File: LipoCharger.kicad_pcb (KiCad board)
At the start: 4 copper layers, 43.5 x 36 mm, 34 parts, among them J1 S2B-XH-A, J2 USB_C_Receptacle_USB2.0_14P, Q1 SI2300A, Q2 SI2300A, SW1 SK12D07VG4, U1 TP4056-42-ESOP8, U2 MT3608, U3 FM2113

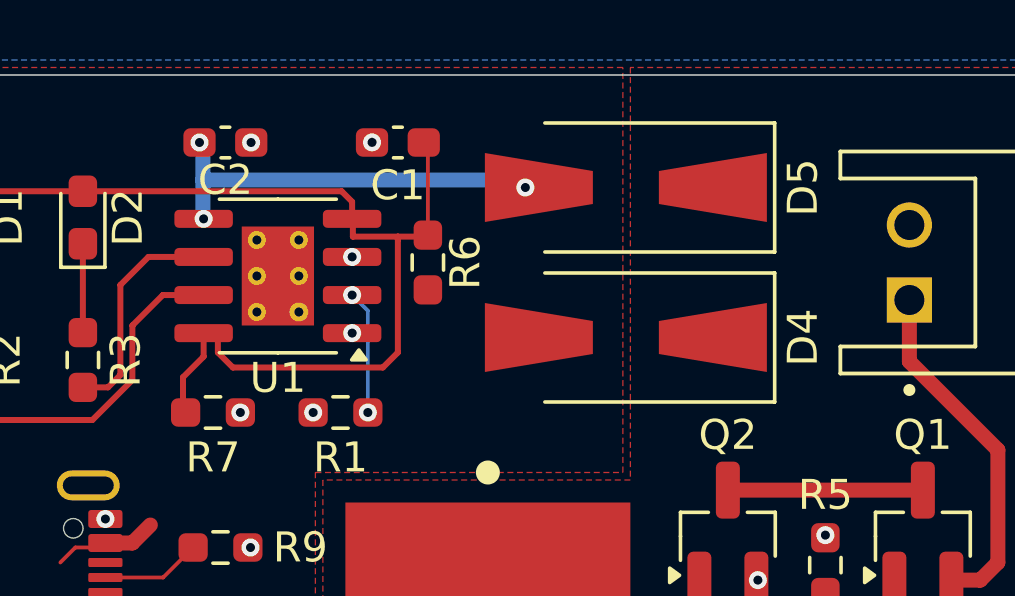
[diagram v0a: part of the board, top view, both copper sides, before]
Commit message: Updated to add power pathing for usb and charging ic
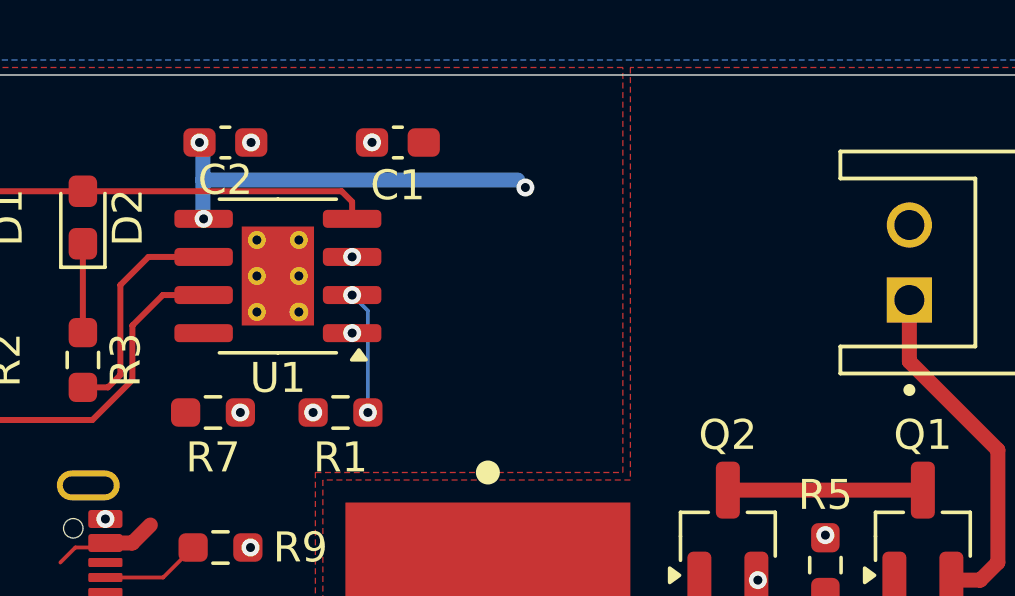
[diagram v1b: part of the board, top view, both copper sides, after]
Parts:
- removed D4, D5: B340A, Diode_SMD:D_SMA-SMB_Universal_Handsoldering
- removed R6: 0.4, Resistor_SMD:R_0603_1608Metric_Pad0.98x0.95mm_HandSolder
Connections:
- C1 pad 1: Net-(D1-A) -> VBUS
- C2 pad 1: Net-(D5-A) -> +BATT
- D1 pad 2: Net-(D1-A) -> VBUS
- D2 pad 2: Net-(D1-A) -> VBUS
- R7 pad 1: Net-(D1-A) -> VBUS
- U1 pad 4: Net-(D1-A) -> VBUS
- U1 pad 5: Net-(D5-A) -> +BATT
- U1 pad 8: Net-(D1-A) -> VBUS
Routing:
- net Net-(D1-A): track 34.2 -> 0.00 mm
- net VBUS: track 7.43 -> 21.9 mm
- net Net-(D5-A): track 13.6 -> 0.00 mm, vias 3 -> 0
- net +BATT: track 6.47 -> 20.1 mm, vias 0 -> 3

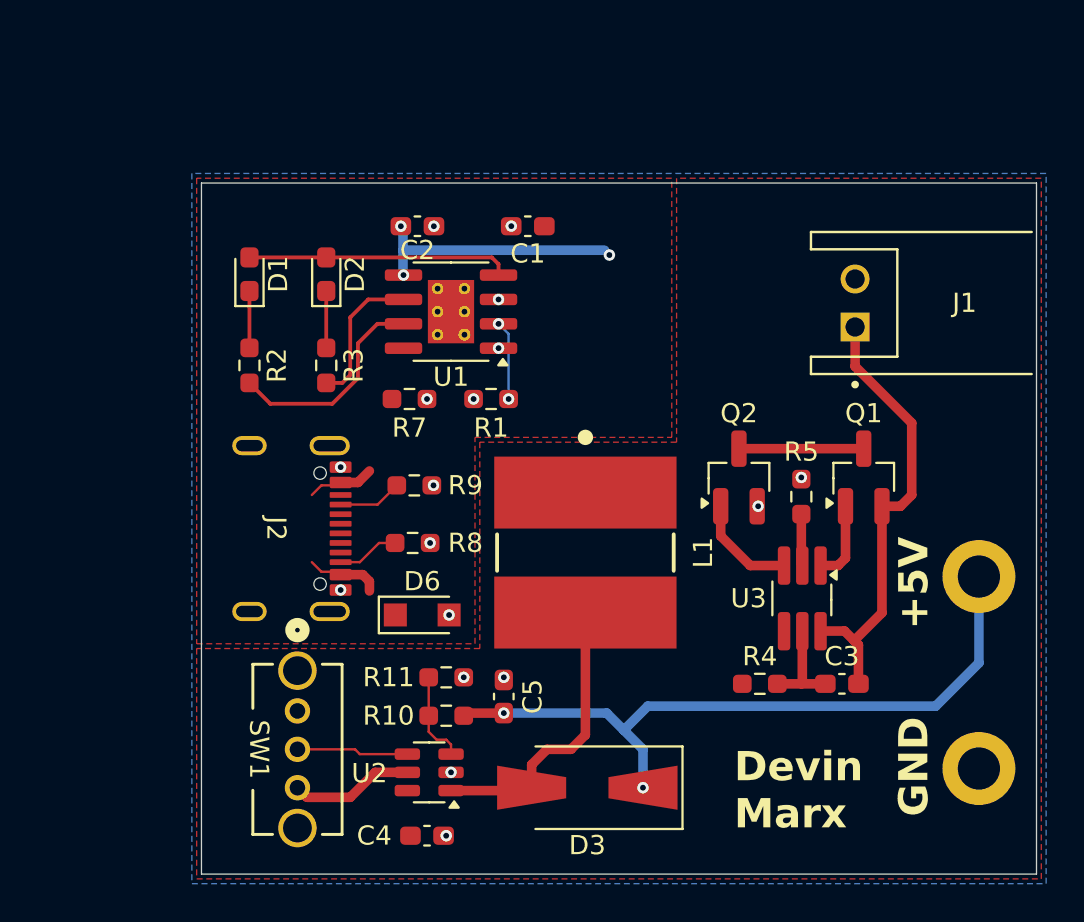
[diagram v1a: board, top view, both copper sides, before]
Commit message: added the updated inductor and update the model for the PMOS mosfet (Should update the NMOS)
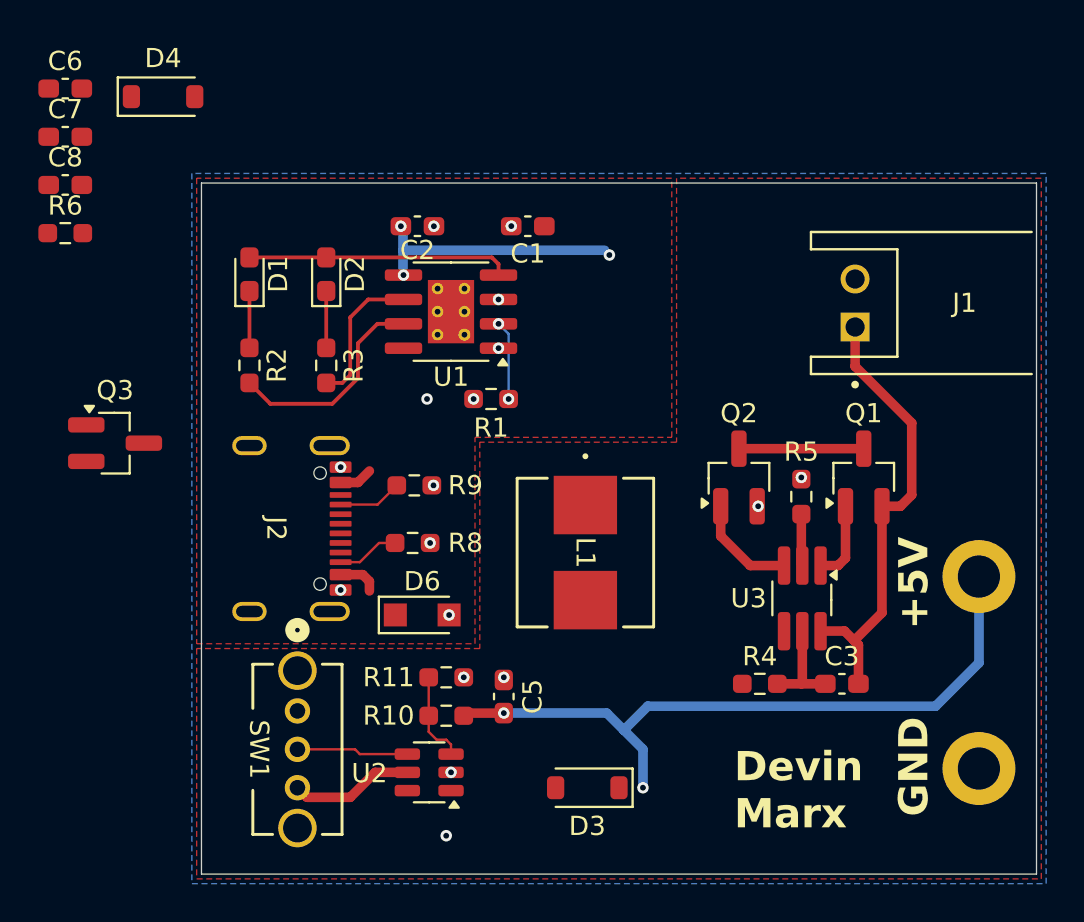
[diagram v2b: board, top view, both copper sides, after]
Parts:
- removed C4: 22uF, Capacitor_SMD:C_0603_1608Metric_Pad1.08x0.95mm_HandSolder
- removed R7: 10k, Resistor_SMD:R_0603_1608Metric_Pad0.98x0.95mm_HandSolder
- added C6: 100nF, Capacitor_SMD:C_0603_1608Metric_Pad1.08x0.95mm_HandSolder, F.Cu at (22.9, 19.6)
- added C7: 100nF, Capacitor_SMD:C_0603_1608Metric_Pad1.08x0.95mm_HandSolder, F.Cu at (22.9, 22.1)
- added C8: 22uF, Capacitor_SMD:C_0603_1608Metric_Pad1.08x0.95mm_HandSolder, F.Cu at (22.9, 24.6)
- added D4: MBR230LSFT1G, Diode_SMD:D_SOD-123, F.Cu at (28.0, 20.0)
- added Q3: HL 2305A, Package_TO_SOT_SMD:SOT-23_Handsoldering, F.Cu at (25.5, 38.0)
- added R6: 10k, Resistor_SMD:R_0603_1608Metric_Pad0.98x0.95mm_HandSolder, F.Cu at (22.9, 27.1)
- C1, C2: value 10uF -> 22uF
- C3: value 0.1uF -> 100nF
- D3: value SS34 -> MBR230LSFT1G; footprint Diode_SMD:D_SMA-SMB_Universal_Handsoldering -> Diode_SMD:D_SOD-123
- L1: value 22uH -> 10uH; footprint a_Library:WE-PD2_1054 -> a_Library:HY0630-100M-M
- R10: value 73.2k -> 82k
- R11: value 10k -> 11k
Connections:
- L1 pad 1: +BATT -> Net-(D4-K)
- U2 pad 5: +BATT -> Net-(D4-K)
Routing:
- net Net-(D3-A): track 14.1 -> 0.00 mm
- net VBUS: track 21.9 -> 18.8 mm

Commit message: Reoriented the PCB for the updated schematic layout
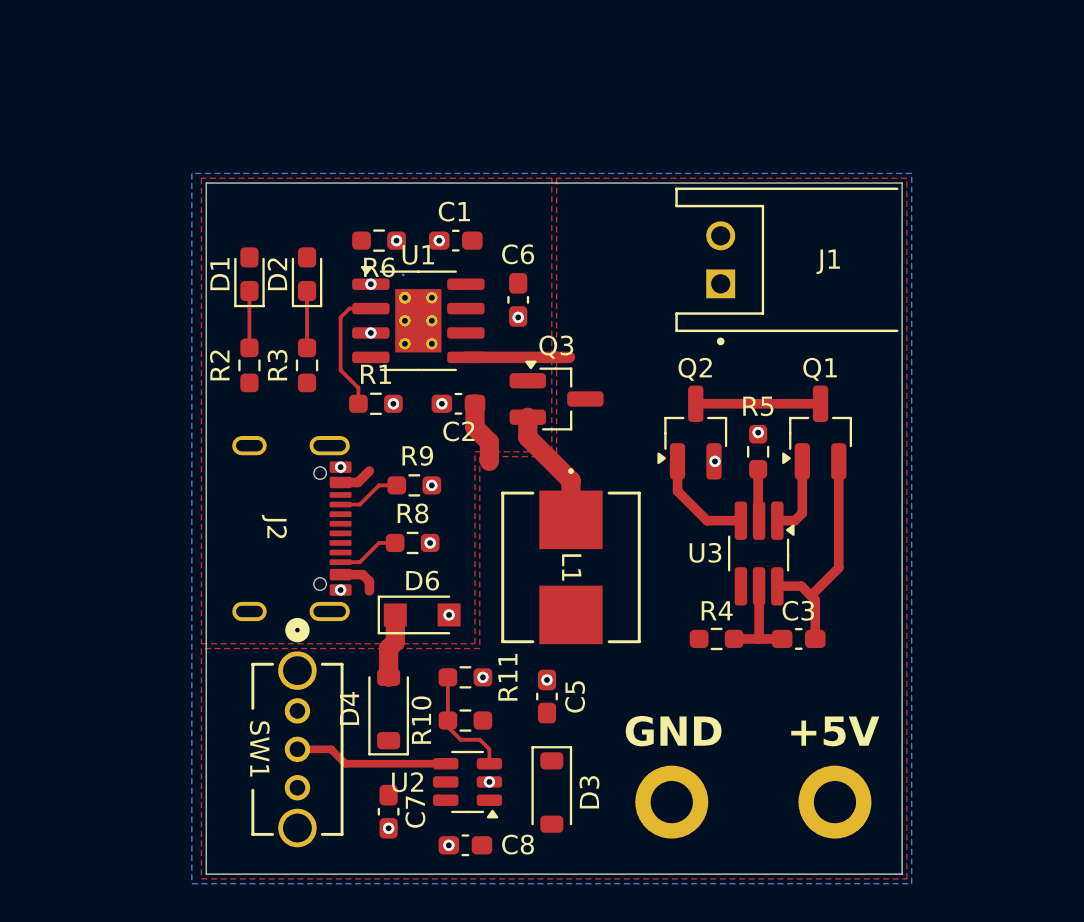
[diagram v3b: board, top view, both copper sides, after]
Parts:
- moved C8 40.2 mm to (43.8, 59.0), turned to 180 degrees
- moved C7 39.0 mm to (39.8, 57.2), turned to -90 degrees
- moved D4 34.0 mm to (39.8, 51.9), turned to 90 degrees
- moved C6 26.0 mm to (46.5, 30.6), turned to -90 degrees
- moved Q3 23.1 mm to (48.5, 35.8)
- moved R6 16.3 mm to (39.2, 27.5), turned to 180 degrees
- moved GND_OUT1 16.1 mm to (53.5, 55.0)
- moved PWR_OUT1 13.9 mm to (62.0, 55.8)
- moved C2 9.49 mm to (43.4, 36.0), turned to 180 degrees
- moved J1 7.35 mm to (62.8, 28.5)
- moved Devin M. 7.16 mm to (59.0, 44.5)
- moved R1 6.01 mm to (39.1, 36.0), turned to 0 degrees
- moved C1 3.82 mm to (43.2, 27.5)
- moved U3 3.24 mm to (59.0, 43.8)
- moved C3 3.24 mm to (61.1, 48.2)
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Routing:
- net Net-(D3-K): track 36.6 -> 0.00 mm, vias 2 -> 0
- net -BATT: track 23.9 -> 11.9 mm
- net Net-(U1-~{CHRG}): track 11.3 -> 0.00 mm
- net +BATT: track 20.1 -> 8.86 mm, vias 3 -> 0
- net VBUS: track 18.8 -> 8.29 mm
- net Net-(U1-~{STDBY}): track 7.58 -> 0.14 mm
- net Net-(D4-K): track 0.00 -> 6.28 mm
- net Net-(U1-PROG): track 4.27 -> 6.65 mm, vias 2 -> 0
- net Net-(U2-EN): track 5.83 -> 8.04 mm
- net Net-(U2-FB): track 4.77 -> 5.98 mm
- net GND: track 0.65 -> 0.31 mm, vias 17 -> 19
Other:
- board size 43.5 x 36 mm -> 36.2 x 36 mm
- board text added: "+5v"
- board text removed: "Devin Marx"

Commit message: Routed some traces (Almost finished routing)
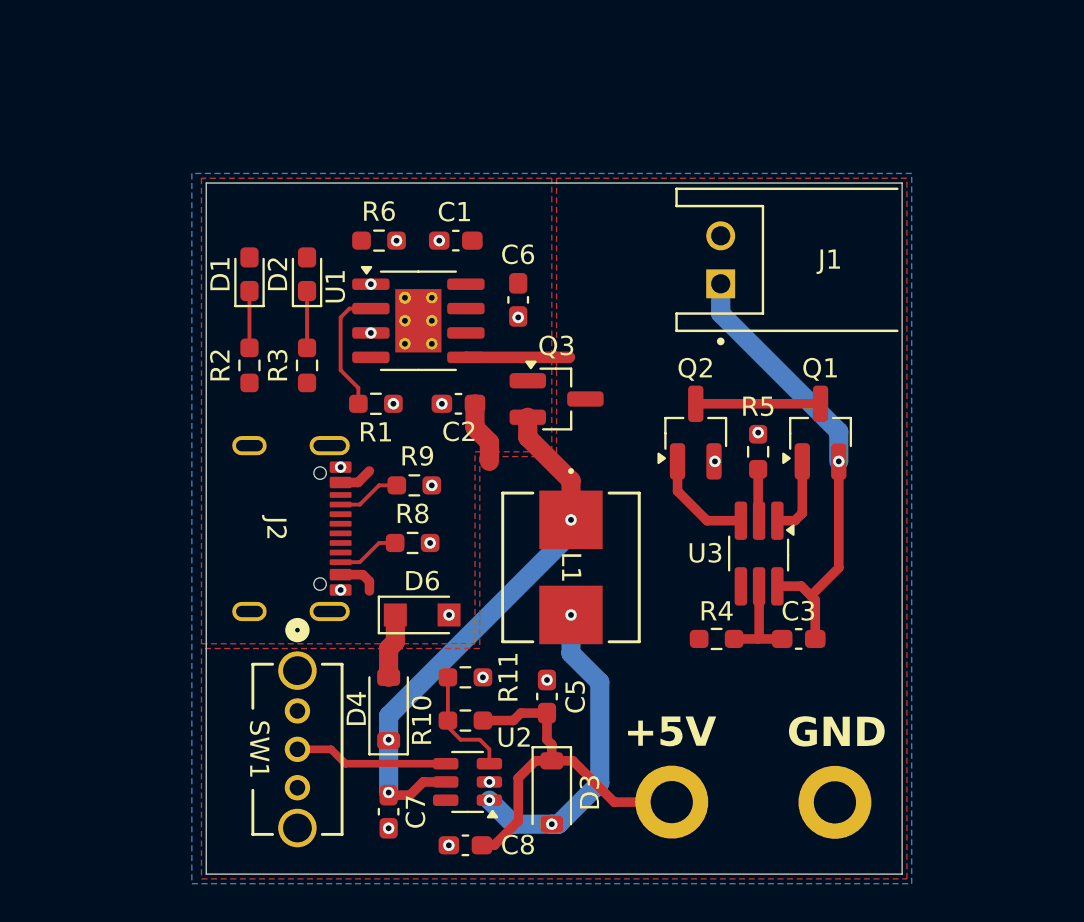
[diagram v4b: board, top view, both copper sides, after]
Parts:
- moved GND_OUT1 9.66 mm to (63.0, 56.8)
- moved PWR_OUT1 7.57 mm to (54.5, 56.8)
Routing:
- net Net-(D4-K): track 6.28 -> 27.7 mm, vias 0 -> 3
- net Net-(D3-K): track 0.00 -> 20.0 mm
- net Net-(D3-A): track 0.00 -> 16.5 mm, vias 0 -> 3
- net -BATT: track 11.9 -> 23.7 mm, vias 0 -> 1

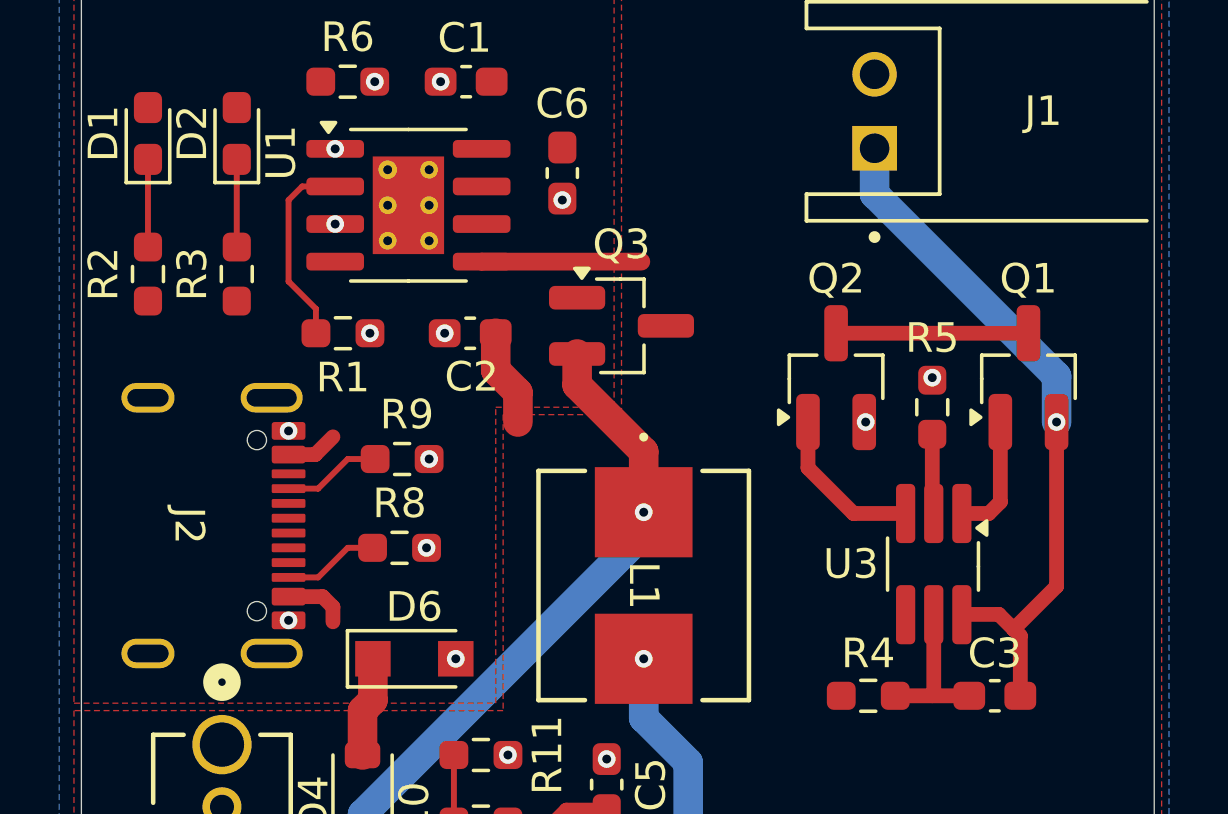
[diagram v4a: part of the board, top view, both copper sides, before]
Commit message: fixed nmos footprints
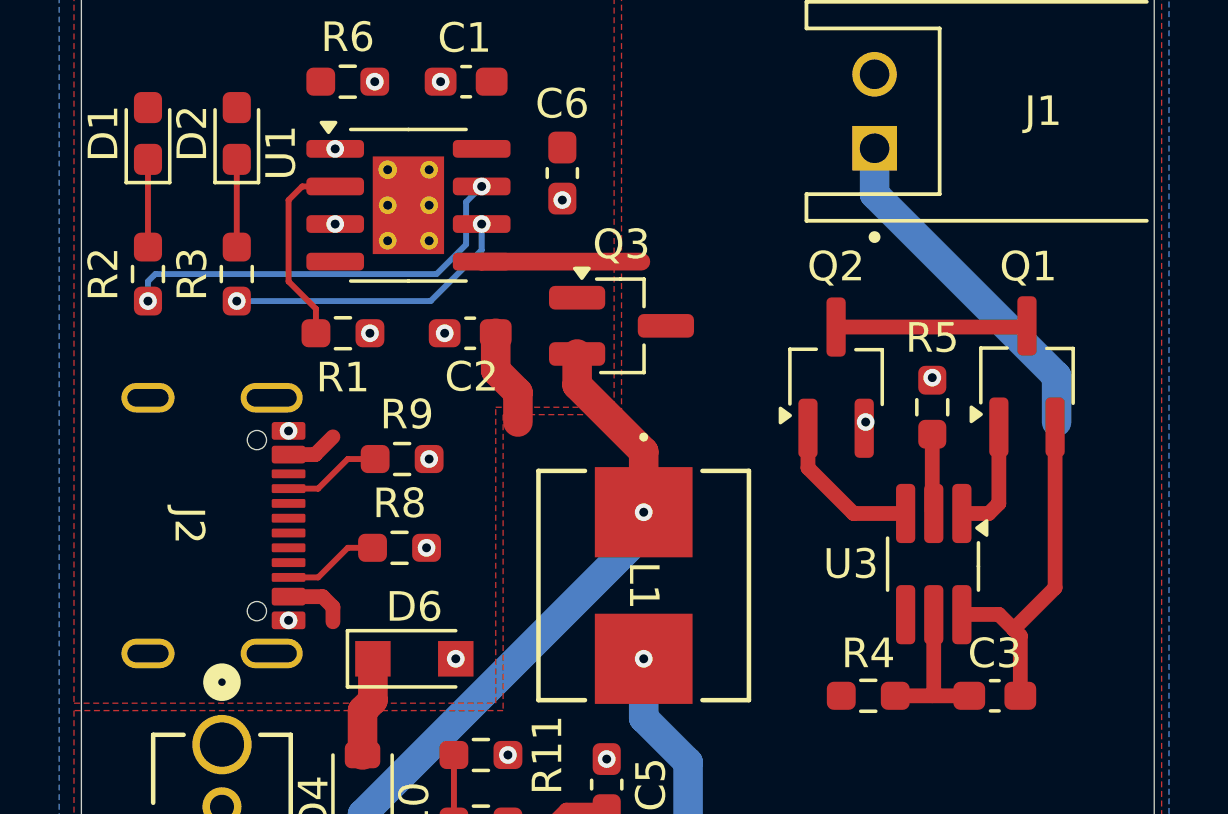
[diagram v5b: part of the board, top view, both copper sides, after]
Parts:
- Q1, Q2: footprint Package_TO_SOT_SMD:SOT-23_Handsoldering -> Package_TO_SOT_SMD:TSOT-23_HandSoldering
- moved Q1 0.06 mm to (62.2, 37.5)
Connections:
- Q1 pad 1: Net-(Q1-D) -> Net-(Q1-G)
- Q1 pad 2: Net-(Q1-G) -> -BATT
- Q1 pad 3: -BATT -> Net-(Q1-D)
- Q2 pad 1: Net-(Q1-D) -> Net-(Q2-G)
- Q2 pad 2: Net-(Q2-G) -> GND
- Q2 pad 3: GND -> Net-(Q1-D)
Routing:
- net Net-(U1-~{CHRG}): track 0.00 -> 14.1 mm, vias 0 -> 2
- net Net-(U1-~{STDBY}): track 0.14 -> 10.0 mm, vias 0 -> 2
- net -BATT: track 23.7 -> 23.5 mm, vias 1 -> 0
